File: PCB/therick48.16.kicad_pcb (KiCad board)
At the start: 2 copper layers, 308.9 x 75.8 mm, 173 parts, among them J1 TYPE-C-31-M12_13, J2 AVR-ISP-6_mod, K1 KEYSW, K10 KEYSW, K11 KEYSW, K12 KEYSW, K13 KEYSW, K14 KEYSW, K15 KEYSW, K16 KEYSW, K17 KEYSW, K18 KEYSW, K19 KEYSW, K2 KEYSW, K20 KEYSW, K21 KEYSW, K22 KEYSW, K23 KEYSW, K24 KEYSW, K25 KEYSW, K26 KEYSW, K27 KEYSW, K28 KEYSW, K29 KEYSW, K3 KEYSW, K30 KEYSW, K31 KEYSW, K32 KEYSW, K33 KEYSW, K34 KEYSW, K35 KEYSW, K36 KEYSW, K37 KEYSW, K38 KEYSW, K39 KEYSW, K4 KEYSW, K40 KEYSW, K41 KEYSW, K42 KEYSW, K43 KEYSW, K44 KEYSW, K45 KEYSW, K46 KEYSW, K47 KEYSW, K48 KEYSW, K49 KEYSW, K5 KEYSW, K50 KEYSW, K51 KEYSW, K52 KEYSW, K53 KEYSW, K54 KEYSW, K55 KEYSW, K56 KEYSW, K57 KEYSW, K58 KEYSW, K59 KEYSW, K6 KEYSW, K60 KEYSW, K61 KEYSW, K62 KEYSW, K63 KEYSW, K64 KEYSW, K7 KEYSW, K8 KEYSW, K9 KEYSW, SW1 SW_PUSH, U1 ATMEGA32U4, U2 HOLE, U3 USBLC6-2SC6, U4 HOLE, U5 HOLE, U6 HOLE, U7 HOLE, U8 HOLE, Y1 16MHz

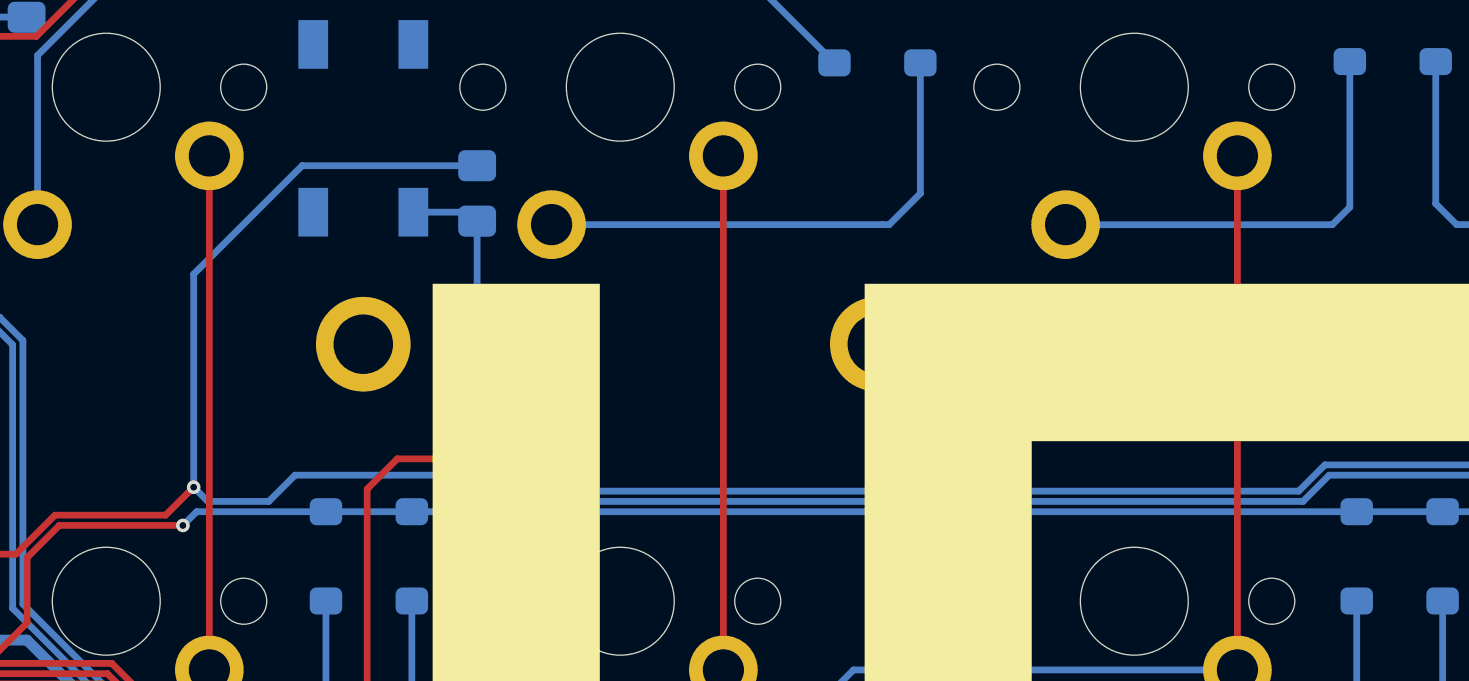
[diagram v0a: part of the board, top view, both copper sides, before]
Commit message: Changed a trace
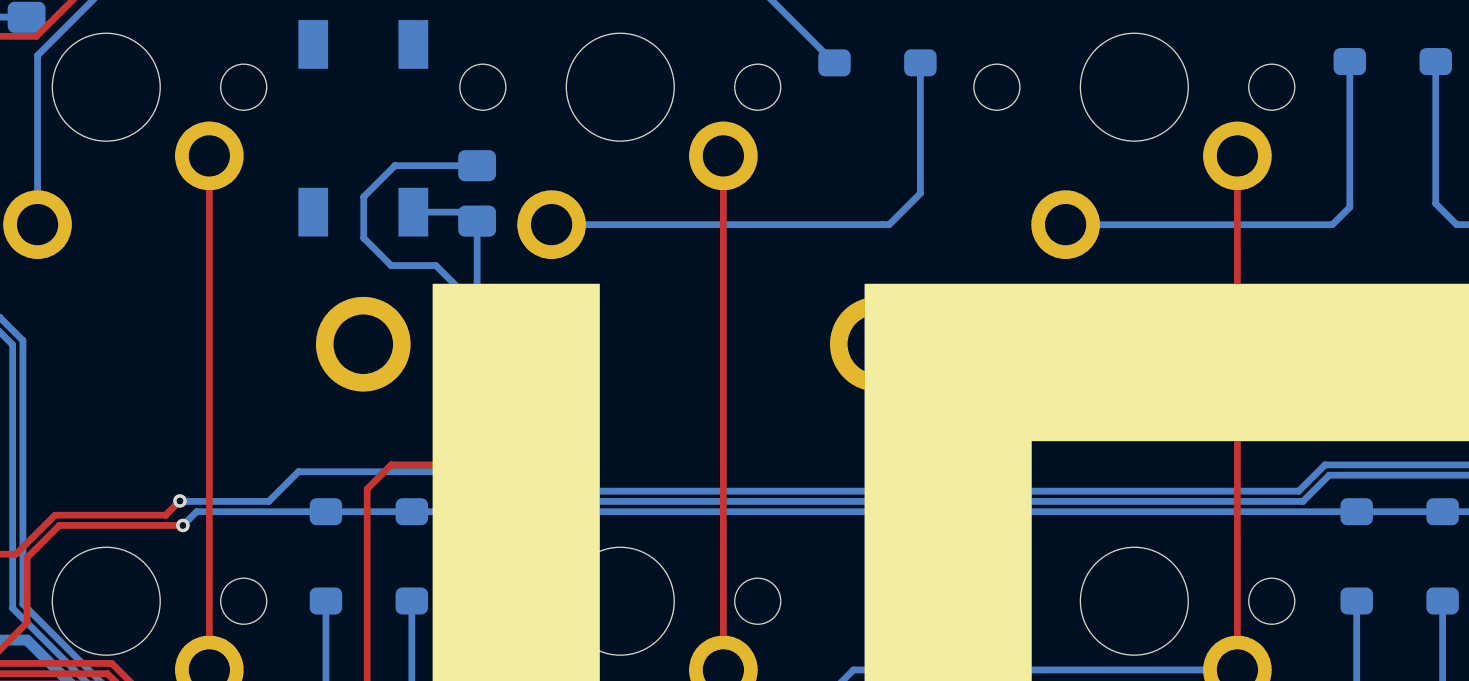
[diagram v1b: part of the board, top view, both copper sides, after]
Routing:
- net VCC: track 218.1 -> 215.1 mm
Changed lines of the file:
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@@
     (thickness 1.6)
     (drawings 84)
-    (tracks 844)
+    (tracks 848)
     (zones 0)
     (modules 173)
@@
     (35 F.Paste user)
     (36 B.SilkS user)
-    (37 F.SilkS user)
+    (37 F.SilkS user hide)
     (38 B.Mask user)
     (39 F.Mask user)
@@
     (add_net "Net-(D9-Pad2)")
     (add_net "Net-(J1-PadA5)")
-    (add_net "Net-(J1-PadA8)")
     (add_net "Net-(J1-PadB5)")
-    (add_net "Net-(J1-PadB8)")
     (add_net "Net-(R1-Pad2)")
     (add_net "Net-(R2-Pad1)")
     (add_net "Net-(R3-Pad1)")
-    (add_net "Net-(U1-Pad18)")
-    (add_net "Net-(U1-Pad19)")
-    (add_net "Net-(U1-Pad20)")
-    (add_net "Net-(U1-Pad21)")
-    (add_net "Net-(U1-Pad32)")
-    (add_net "Net-(U1-Pad42)")
     (add_net VBUS)
     (add_net VCC)
@@
   )
   (dimension 308.94 (width 0.05) (layer Dwgs.User)
-    (gr_text "308.940 mm" (at 201.210106 12.515382 360) (layer Dwgs.User)
+    (gr_text "308.940 mm" (at 201.210106 12.515382) (layer Dwgs.User)
       (effects (font (size 1 1) (thickness 0.15)))
     )
@@
   (segment (start 91.58322 60.279365) (end 90.140586 61.722) (width 0.25) (layer F.Cu) (net 49))
   (segment (start 95.676635 60.279365) (end 91.58322 60.279365) (width 0.25) (layer F.Cu) (net 49))
-  (segment (start 96.7105 59.2455) (end 95.676635 60.279365) (width 0.25) (layer F.Cu) (net 49))
   (segment (start 90.140586 61.722) (end 87.884 61.722) (width 0.25) (layer F.Cu) (net 49))
   (segment (start 85.3505 64.219) (end 86.825 64.219) (width 0.4) (layer B.Cu) (net 49))
@@
   (segment (start 86.825 62.781) (end 87.884 61.722) (width 0.25) (layer B.Cu) (net 49))
   (segment (start 86.825 64.219) (end 86.825 62.781) (width 0.25) (layer B.Cu) (net 49))
-  (via (at 96.7105 59.2455) (size 0.5) (drill 0.25) (layers F.Cu B.Cu) (net 49))
-  (segment (start 99.486635 59.771365) (end 97.236365 59.771365) (width 0.25) (layer B.Cu) (net 49))
-  (segment (start 100.457 58.801) (end 99.486635 59.771365) (width 0.25) (layer B.Cu) (net 49))
-  (segment (start 106.888365 59.771365) (end 105.918 58.801) (width 0.25) (layer B.Cu) (net 49))
-  (segment (start 160.1832 50.15) (end 161.87 50.15) (width 0.25) (layer B.Cu) (net 49))
-  (segment (start 144.018 58.801) (end 138.684 58.801) (width 0.25) (layer B.Cu) (net 49))
-  (segment (start 105.918 58.801) (end 100.457 58.801) (width 0.25) (layer B.Cu) (net 49))
-  (segment (start 137.713635 59.771365) (end 106.888365 59.771365) (width 0.25) (layer B.Cu) (net 49))
-  (segment (start 158.617414 62.32) (end 156.06878 59.771365) (width 0.25) (layer B.Cu) (net 49))
-  (segment (start 97.236365 59.771365) (end 96.7105 59.2455) (width 0.25) (layer B.Cu) (net 49))
+  (via (at 96.2025 59.7535) (size 0.5) (drill 0.25) (layers F.Cu B.Cu) (net 49))
+  (segment (start 96.2025 59.7535) (end 95.676635 60.279365) (width 0.25) (layer F.Cu) (net 49))
+  (segment (start 102.997 50.038) (end 104.013 51.054) (width 0.25) (layer B.Cu) (net 49))
+  (segment (start 104.149 47.362) (end 102.997 48.514) (width 0.25) (layer B.Cu) (net 49))
+  (segment (start 106.68 52.07) (end 106.68 58.674) (width 0.25) (layer B.Cu) (net 49))
+  (segment (start 105.664 51.054) (end 106.68 52.07) (width 0.25) (layer B.Cu) (net 49))
+  (segment (start 104.013 51.054) (end 105.664 51.054) (width 0.25) (layer B.Cu) (net 49))
+  (segment (start 102.997 48.514) (end 102.997 50.038) (width 0.25) (layer B.Cu) (net 49))
+  (segment (start 107.188 47.362) (end 104.149 47.362) (width 0.25) (layer B.Cu) (net 49))
+  (segment (start 99.486635 59.771365) (end 96.220365 59.771365) (width 0.25) (layer B.Cu) (net 49))
+  (segment (start 100.584 58.674) (end 99.486635 59.771365) (width 0.25) (layer B.Cu) (net 49))
+  (segment (start 96.220365 59.771365) (end 96.2025 59.7535) (width 0.25) (layer B.Cu) (net 49))
+  (segment (start 106.68 58.674) (end 100.584 58.674) (width 0.25) (layer B.Cu) (net 49))
+  (segment (start 144.988365 59.771365) (end 144.018 58.801) (width 0.25) (layer B.Cu) (net 49))
+  (segment (start 161.87 50.15) (end 162.26 50.54) (width 0.25) (layer B.Cu) (net 49))
+  (segment (start 137.713635 59.771365) (end 107.777365 59.771365) (width 0.25) (layer B.Cu) (net 49))
   (segment (start 156.06878 59.771365) (end 144.988365 59.771365) (width 0.25) (layer B.Cu) (net 49))
+  (segment (start 158.617414 62.32) (end 156.06878 59.771365) (width 0.25) (layer B.Cu) (net 49))
+  (segment (start 144.018 58.801) (end 138.684 58.801) (width 0.25) (layer B.Cu) (net 49))
+  (segment (start 160.1832 50.15) (end 161.87 50.15) (width 0.25) (layer B.Cu) (net 49))
   (segment (start 161.12 62.32) (end 158.617414 62.32) (width 0.25) (layer B.Cu) (net 49))
   (segment (start 162.26 61.18) (end 161.12 62.32) (width 0.25) (layer B.Cu) (net 49))
-  (segment (start 144.988365 59.771365) (end 144.018 58.801) (width 0.25) (layer B.Cu) (net 49))
-  (segment (start 162.26 50.54) (end 162.26 61.18) (width 0.25) (layer B.Cu) (net 49))
-  (segment (start 161.87 50.15) (end 162.26 50.54) (width 0.25) (layer B.Cu) (net 49))
   (segment (start 138.684 58.801) (end 137.713635 59.771365) (width 0.25) (layer B.Cu) (net 49))
-  (segment (start 100.72 47.362) (end 107.188 47.362) (width 0.25) (layer B.Cu) (net 49))
-  (segment (start 96.7105 51.3715) (end 100.72 47.362) (width 0.25) (layer B.Cu) (net 49))
-  (segment (start 96.7105 59.2455) (end 96.7105 51.3715) (width 0.25) (layer B.Cu) (net 49))
+  (segment (start 162.26 50.54) (end 162.26 61.18) (width 0.25) (layer B.Cu) (net 49))
+  (segment (start 106.68 58.674) (end 107.777365 59.771365) (width 0.25) (layer B.Cu) (net 49))
   (segment (start 91.818394 72.925) (end 90.0375 72.925) (width 0.25) (layer B.Cu) (net 50))
   (segment (start 93.699781 71.043615) (end 91.818394 72.925) (width 0.25) (layer B.Cu) (net 50))
@@
   (segment (start 87.3375 80.425) (end 87.3375 79.425) (width 0.25) (layer B.Cu) (net 79))
   (segment (start 103.124 74.803) (end 103.124 59.309) (width 0.25) (layer F.Cu) (net 79))
-  (segment (start 103.124 59.309) (end 104.23525 58.19775) (width 0.25) (layer F.Cu) (net 79))
   (segment (start 106.856 49.08) (end 107.188 49.412) (width 0.25) (layer B.Cu) (net 79))
   (segment (start 104.83 49.08) (end 106.856 49.08) (width 0.25) (layer B.Cu) (net 79))
-  (segment (start 107.188 58.166) (end 107.21975 58.19775) (width 0.25) (layer B.Cu) (net 79))
-  (via (at 107.21975 58.19775) (size 0.5) (drill 0.25) (layers F.Cu B.Cu) (net 79))
   (segment (start 107.188 49.412) (end 107.188 58.166) (width 0.25) (layer B.Cu) (net 79))
-  (segment (start 104.23525 58.19775) (end 107.21975 58.19775) (width 0.25) (layer F.Cu) (net 79))
+  (via (at 107.188 58.42) (size 0.5) (drill 0.25) (layers F.Cu B.Cu) (net 79))
+  (segment (start 107.188 58.166) (end 107.188 58.42) (width 0.25) (layer B.Cu) (net 79))
+  (segment (start 107.188 58.42) (end 104.013 58.42) (width 0.25) (layer F.Cu) (net 79))
+  (segment (start 103.124 59.309) (end 104.013 58.42) (width 0.25) (layer F.Cu) (net 79))
   (segment (start 156.226185 59.391355) (end 157.144828 60.31) (width 0.25) (layer B.Cu) (net 79))
-  (segment (start 138.526595 58.42099) (end 144.175405 58.42099) (width 0.25) (layer B.Cu) (net 79))
-  (segment (start 137.55623 59.391355) (end 138.526595 58.42099) (width 0.25) (layer B.Cu) (net 79))
   (segment (start 145.145769 59.391355) (end 156.226185 59.391355) (width 0.25) (layer B.Cu) (net 79))
-  (segment (start 108.413355 59.391355) (end 137.55623 59.391355) (width 0.25) (layer B.Cu) (net 79))
-  (segment (start 144.175405 58.42099) (end 145.145769 59.391355) (width 0.25) (layer B.Cu) (net 79))
   (segment (start 157.144828 60.31) (end 159.7768 60.31) (width 0.25) (layer B.Cu) (net 79))
-  (segment (start 107.21975 58.19775) (end 108.413355 59.391355) (width 0.25) (layer B.Cu) (net 79))
+  (segment (start 137.55623 59.391355) (end 138.526595 58.42099) (width 0.25) (layer B.Cu) (net 79))
+  (segment (start 138.526595 58.42099) (end 144.175405 58.42099) (width 0.25) (layer B.Cu) (net 79))
+  (segment (start 108.159355 59.391355) (end 137.55623 59.391355) (width 0.25) (layer B.Cu) (net 79))
+  (segment (start 144.175405 58.42099) (end 145.145769 59.391355) (width 0.25) (layer B.Cu) (net 79))
+  (segment (start 107.188 58.42) (end 108.159355 59.391355) (width 0.25) (layer B.Cu) (net 79))
   (segment (start 297.0393 49.5527) (end 287.3746 49.5527) (width 0.25) (layer B.Cu) (net 80))
   (segment (start 297.92 48.672) (end 297.0393 49.5527) (width 0.25) (layer B.Cu) (net 80))

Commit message: 48+16 to 48.16
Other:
- board text added: "therick48.16"
- board text removed: "therick48+16"
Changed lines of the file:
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@@
     (arrow2b (pts (xy 273.986117 25.852145) (xy 275.111446 25.263473)))
   )
-  (gr_text therick48+16 (at 81.359375 108.299715) (layer B.SilkS)
+  (gr_text therick48.16 (at 81.28 108.299715) (layer B.SilkS)
     (effects (font (size 1.25 1.25) (thickness 0.15)) (justify mirror))
   )
